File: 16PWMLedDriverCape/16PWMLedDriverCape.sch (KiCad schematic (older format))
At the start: 2 parts, among them P8 BeagleBone_Black_Header, P9 BeagleBone_Black_Header

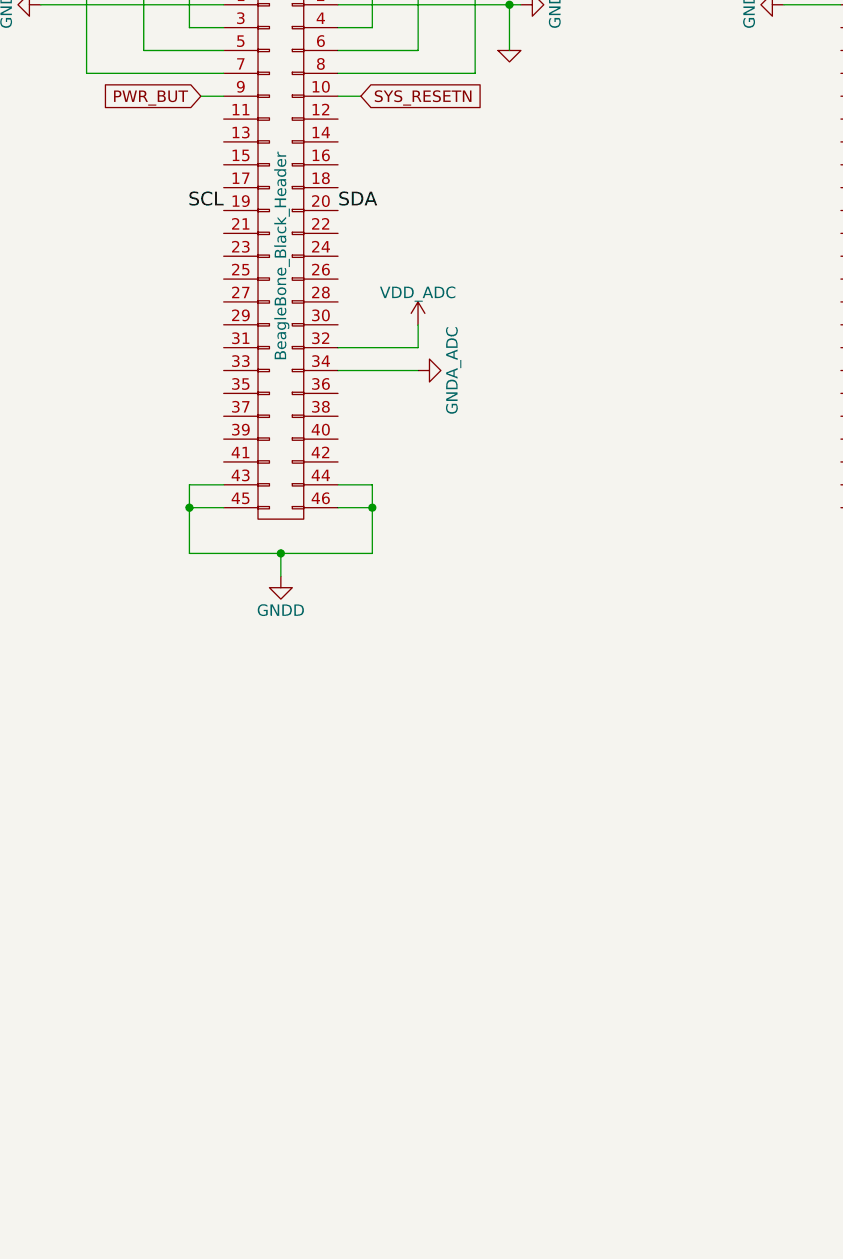
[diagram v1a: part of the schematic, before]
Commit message: Add EEProm to 16PWMLedDriverCape.
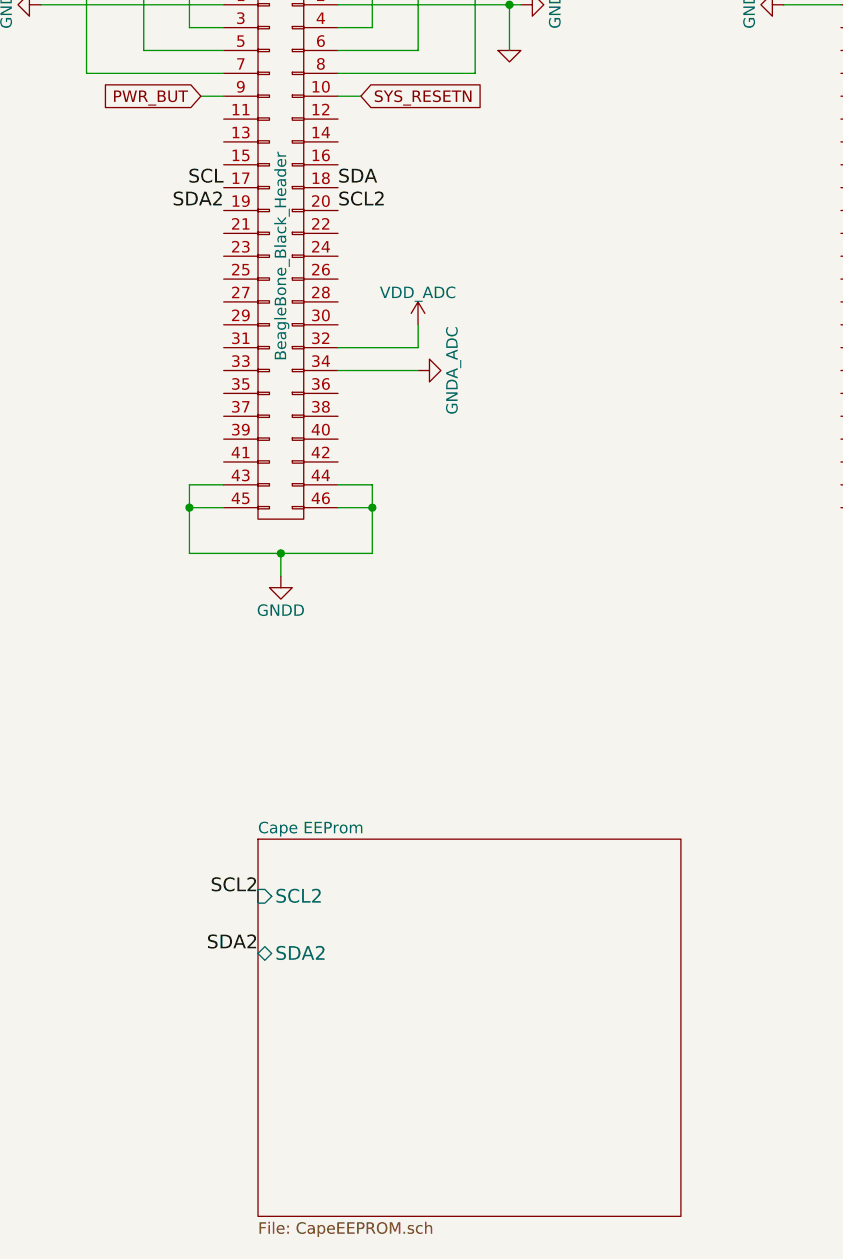
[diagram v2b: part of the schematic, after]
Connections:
- net SCL: now also P9.17 (P17); no longer P9.19 (P19)
- net SDA: now also P9.18 (P18); no longer P9.20 (P20)
- new net SCL2: P9.20 (P20)
- new net SDA2: P9.19 (P19)
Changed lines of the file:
@@
 LIBS:pca9685
 LIBS:tbd62x83a
+LIBS:cat24c256w
 LIBS:16PWMLedDriverCape-cache
 EELAYER 27 0
@@
 $Descr A4 11693 8268
 encoding utf-8
-Sheet 1 2
+Sheet 1 3
 Title ""
-Date "28 mar 2019"
+Date "11 jun 2019"
 Rev ""
 Comp ""
@@
 F4 "OE" I L 7500 3700 60
 $EndSheet
-Text Label 2200 2050 2    60   ~ 0
+Text Label 2200 1950 2    60   ~ 0
 SCL
-Text Label 2700 2050 0    60   ~ 0
+Text Label 2700 1950 0    60   ~ 0
 SDA
 Text Label 7500 3400 2    60   ~ 0
@@
 	3450 1350 3450 1150
 Connection ~ 3450 1150
+$Sheet
+S 2350 4800 1850 1650
+U 5C719AD8
+F0 "Cape EEProm" 50
+F1 "CapeEEPROM.sch" 50
+F2 "SCL2" I L 2350 5050 60
+F3 "SDA2" B L 2350 5300 60
+$EndSheet
+Text Label 2200 2050 2    60   ~ 0
+SDA2
+Text Label 2700 2050 0    60   ~ 0
+SCL2
+Text Label 2350 5050 2    60   ~ 0
+SCL2
+Text Label 2350 5300 2    60   ~ 0
+SDA2
 $EndSCHEMATC

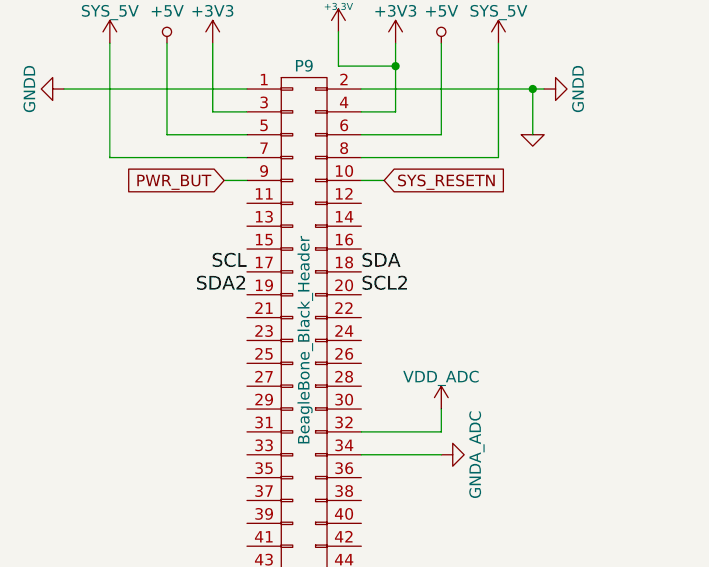
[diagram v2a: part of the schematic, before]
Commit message: Also fix swapped I2C lines in 16PWMLedDriverCape.
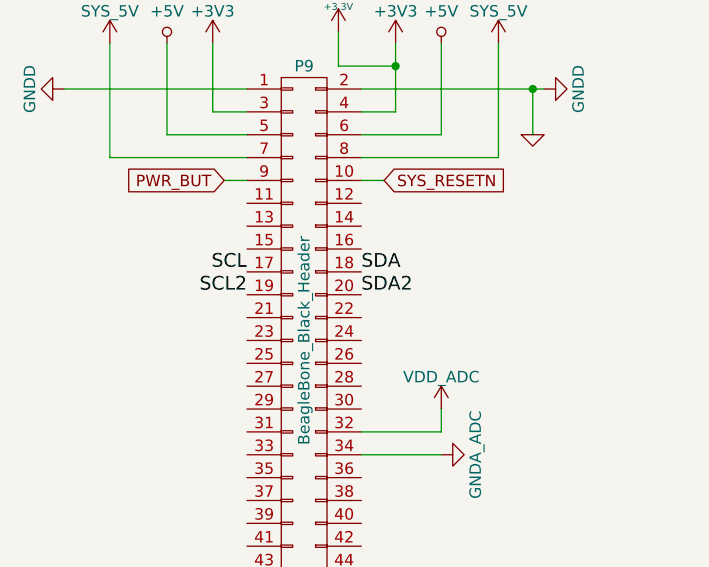
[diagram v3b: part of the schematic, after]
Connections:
- net SCL2: now also P9.19 (P19); no longer P9.20 (P20)
- net SDA2: now also P9.20 (P20); no longer P9.19 (P19)
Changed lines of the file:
@@
 Sheet 1 3
 Title ""
-Date "11 jun 2019"
+Date "4 jul 2019"
 Rev ""
 Comp ""
@@
 F3 "SDA2" B L 2350 5300 60
 $EndSheet
+Text Label 2700 2050 0    60   ~ 0
+SDA2
 Text Label 2200 2050 2    60   ~ 0
-SDA2
-Text Label 2700 2050 0    60   ~ 0
 SCL2
 Text Label 2350 5050 2    60   ~ 0
